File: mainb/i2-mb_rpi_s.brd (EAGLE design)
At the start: 110 x 106.6 mm, 36 parts, among them IC3 DS1307Z, T1 BC337, T2 BC337, X9 eth (mb->rpi)

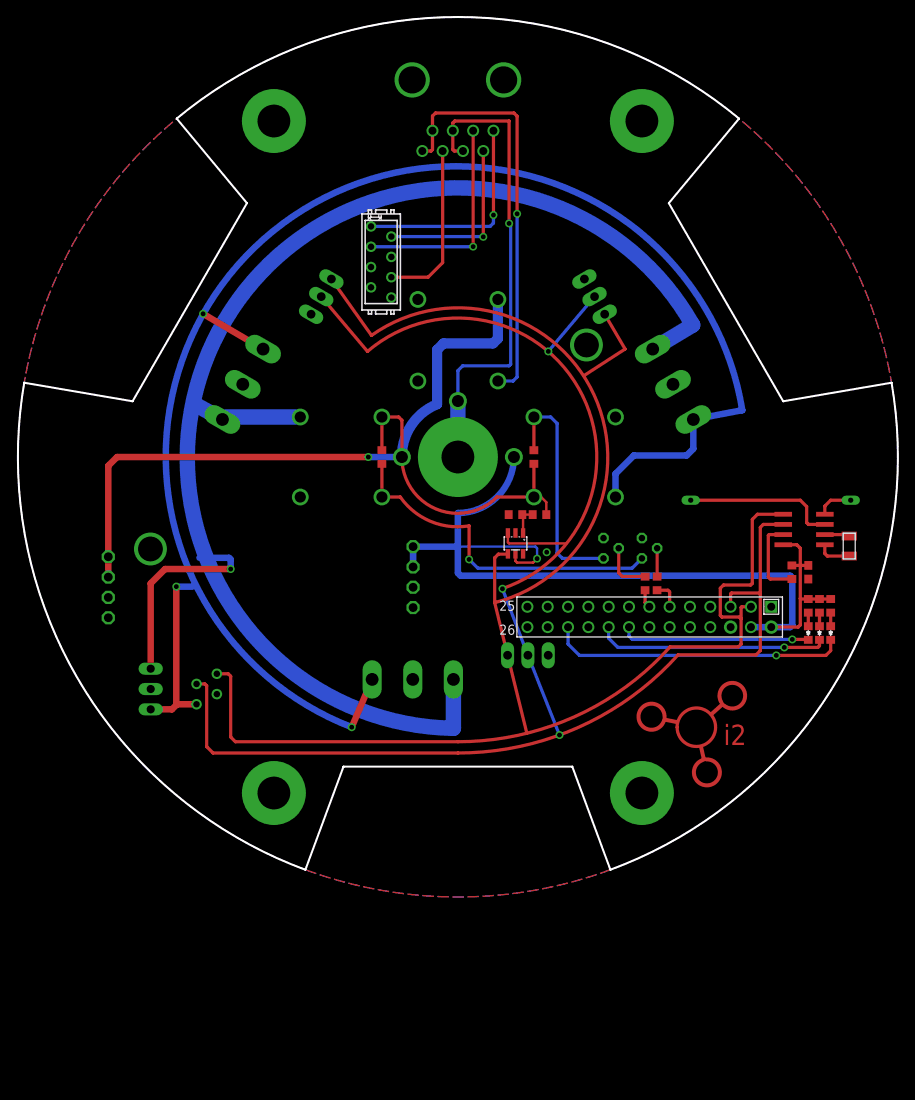
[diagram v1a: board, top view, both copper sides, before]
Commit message: /mainb: 1) pins on relays
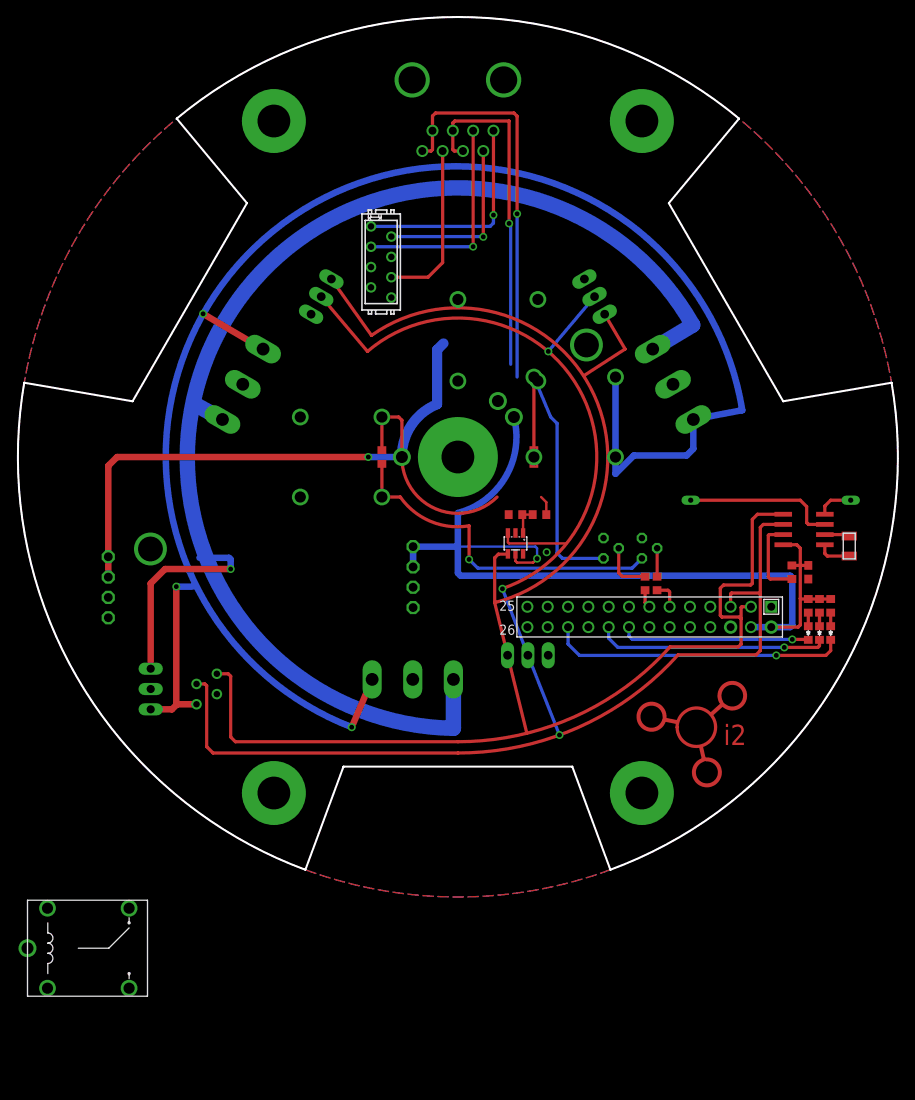
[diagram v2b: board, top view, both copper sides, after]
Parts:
- added U$9: FBR51, wb:PC_RELAY
- moved U$5 5.00 mm to (7.00, 5.00)
- moved U$6 5.00 mm to (5.00, 7.00)
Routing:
- net +12V_IN: track 115.3 -> 94.6 mm
- net AKU+: track 60.0 -> 42.3 mm
- net +12V_OUT: track 110.7 -> 101.3 mm
- net +5V: track 124.7 -> 133.9 mm
- net N$2: track 29.7 -> 38.0 mm
- net +5V_RPI: track 115.6 -> 119.6 mm
- net POE-: track 51.6 -> 49.0 mm
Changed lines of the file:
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@@
 <?xml version="1.0" encoding="utf-8"?>
 <!DOCTYPE eagle SYSTEM "eagle.dtd">
-<eagle version="6.4">
+<eagle version="6.5.0">
 <drawing>
 <settings>
@@
 <element name="R1" library="rcl" package="R0603" value="? 1%" x="10.2" y="-7.2" smashed="yes" rot="R180"/>
 <element name="R2" library="rcl" package="R0603" value="? 1%" x="7.2" y="-7.2" smashed="yes" rot="R180"/>
-<element name="U$6" library="wb" package="PC_RELAY" value="FBR51" x="0" y="7" smashed="yes" rot="MR90"/>
+<element name="U$6" library="wb" package="PC_RELAY" value="FBR51" x="5" y="7" smashed="yes" rot="MR90"/>
 <element name="U$7" library="wb" package="PC_RELAY" value="FBR51" x="-7" y="0" smashed="yes" rot="MR0"/>
 <element name="X_ETH" library="con-maritex" package="8P8C-TOP" value="eth (PC-&gt;mb)" x="0" y="44.6" smashed="yes" rot="R90"/>
 <element name="R3" library="rcl" package="R0603" value="4k7" x="23.4" y="-15.8" smashed="yes" rot="R90"/>
 <element name="U$3" library="wojtkowa" package="D0603" value="1N4148" x="9.5" y="0" smashed="yes" rot="R270"/>
-<element name="U$5" library="wb" package="PC_RELAY" value="FBR51" x="7" y="0" smashed="yes" rot="MR180"/>
+<element name="U$5" library="wb" package="PC_RELAY" value="FBR51" x="7" y="5" smashed="yes" rot="MR180"/>
 <element name="U$8" library="pololu" package="POLOLU-2111" value="POLOLU-2111" x="-25.92" y="-15.01" smashed="yes" rot="MR180"/>
 <element name="IC3" library="ds1307_pcf8583" package="SOIC8" value="DS1307Z" x="43.27" y="-9.06" smashed="yes" rot="R90">
@@
 </element>
 <element name="U$1" library="isfar2-logo" package="I2-LOGO" value="" x="30" y="-33.4"/>
+<element name="U$9" library="wb" package="PC_RELAY" value="FBR51" x="-53.8" y="-61.4"/>
 </elements>
 <signals>
@@
 <contactref element="X_ETH" pad="8"/>
 <contactref element="U$6" pad="C+"/>
-<wire x1="5" y1="9.5" x2="6.9" y2="9.5" width="0.4064" layer="16"/>
-<wire x1="6.9" y1="9.5" x2="7.4" y2="10" width="0.4064" layer="16"/>
+<wire x1="10" y1="9.5" x2="6.9" y2="9.5" width="0" layer="19" extent="1-16"/>
+<wire x1="6.9" y1="9.5" x2="7.4" y2="10" width="0" layer="19" extent="1-16"/>
 <wire x1="7.4" y1="10" x2="7.4" y2="30.4" width="0.4064" layer="16"/>
 <via x="7.4" y="30.4" extent="1-16" drill="0.6"/>
@@
 <wire x1="-2.6" y1="6.6" x2="-2.6" y2="13.4" width="1.27" layer="16"/>
 <wire x1="-2.6" y1="13.4" x2="-1.8" y2="14.2" width="1.27" layer="16"/>
-<wire x1="-1.8" y1="14.2" x2="4.4" y2="14.2" width="1.27" layer="16"/>
-<wire x1="4.4" y1="14.2" x2="5" y2="14.8" width="1.27" layer="16"/>
-<wire x1="5" y1="19.7" x2="5" y2="14.8" width="1.27" layer="16"/>
 <wire x1="-43.7" y1="-15.01" x2="-43.7" y2="-12.47" width="0.8128" layer="1"/>
 <wire x1="-43.7" y1="-12.47" x2="-43.7" y2="-1.1" width="0.8128" layer="1"/>
@@
 <wire x1="-7" y1="0" x2="-2.6" y2="6.6" width="1.27" layer="16" curve="-68.498566"/>
 <wire x1="-9.5" y1="5" x2="-9.5" y2="0.85" width="0.4064" layer="1"/>
-<wire x1="9.5" y1="-0.85" x2="9.5" y2="-5" width="0.4064" layer="1"/>
-<wire x1="9.5" y1="-5" x2="4.9" y2="-5" width="0.4064" layer="1"/>
+<wire x1="9.5" y1="-0.85" x2="9.5" y2="0" width="0.4064" layer="1"/>
+<wire x1="9.5" y1="0" x2="4.9" y2="-5" width="0" layer="19" extent="1-16"/>
 <wire x1="-7" y1="0" x2="4.9" y2="-5" width="0.4064" layer="1" curve="135.578726"/>
 <wire x1="-7" y1="0" x2="-7" y2="4.6" width="0.4064" layer="1"/>
@@
 <wire x1="10.4" y1="-5" x2="11.05" y2="-5.65" width="0.3048" layer="1"/>
 <wire x1="11.05" y1="-7.2" x2="11.05" y2="-5.65" width="0.3048" layer="1"/>
-<wire x1="10.4" y1="-5" x2="9.5" y2="-5" width="0.3048" layer="1"/>
+<wire x1="10.4" y1="-5" x2="9.5" y2="0" width="0" layer="19" extent="1-16"/>
+<wire x1="-1.8" y1="14.2" x2="0" y2="19.7" width="0" layer="19" extent="16-16"/>
 </signal>
 <signal name="+5V" airwireshidden="yes">
@@
 <wire x1="-24.35" y1="13.48940625" x2="-31.85" y2="17.9" width="0.8128" layer="1"/>
 <via x="-31.85" y="17.9" extent="1-16" drill="0.6"/>
-<wire x1="19.7" y1="-5" x2="19.7" y2="-2.1" width="0.8128" layer="16"/>
+<wire x1="19.7" y1="10" x2="19.7" y2="-2.1" width="0.8128" layer="16"/>
 <wire x1="19.7" y1="-2.1" x2="22" y2="0.2" width="0.8128" layer="16"/>
 <wire x1="22" y1="0.2" x2="28.6" y2="0.2" width="0.8128" layer="16"/>
@@
 <contactref element="I2C_3" pad="3"/>
 <contactref element="I2C_1" pad="3"/>
+<wire x1="8.15" y1="-12.1001" x2="7.2" y2="-9.4999" width="0" layer="19" extent="1-1"/>
 </signal>
 <signal name="N$1">
@@
 <contactref element="U$5" pad="C-"/>
 <contactref element="T2" pad="3"/>
-<wire x1="9.5" y1="5" x2="9.5" y2="0.85" width="0.4064" layer="1"/>
+<wire x1="9.5" y1="10" x2="9.5" y2="0.85" width="0.4064" layer="1"/>
 <wire x1="18.2" y1="-12.67" x2="13.07" y2="-12.67" width="0.4064" layer="16"/>
 <wire x1="13.07" y1="-12.67" x2="12.4" y2="-12" width="0.4064" layer="16"/>
 <wire x1="12.4" y1="-12" x2="12.4" y2="4.2" width="0.4064" layer="16"/>
 <wire x1="12.4" y1="4.2" x2="11.6" y2="5" width="0.4064" layer="16"/>
-<wire x1="9.5" y1="5" x2="11.6" y2="5" width="0.4064" layer="16"/>
+<wire x1="9.5" y1="10" x2="11.6" y2="5" width="0.4064" layer="16"/>
 </signal>
 <signal name="REL1">
@@
 <contactref element="X_ETH" pad="5"/>
 <via x="0" y="0" extent="1-16" drill="4.1" diameter="10"/>
-<wire x1="0" y1="0" x2="0" y2="7" width="1.9304" layer="16"/>
-<wire x1="0" y1="7" x2="0" y2="10.8" width="0.4064" layer="16"/>
-<wire x1="0" y1="10.8" x2="0.6" y2="11.4" width="0.4064" layer="16"/>
-<wire x1="0.6" y1="11.4" x2="6.4" y2="11.4" width="0.4064" layer="16"/>
-<wire x1="6.4" y1="11.4" x2="6.6" y2="11.6" width="0.4064" layer="16"/>
+<wire x1="0" y1="0" x2="5" y2="7" width="0" layer="19" extent="1-16"/>
+<wire x1="5" y1="7" x2="0" y2="10.8" width="0" layer="19" extent="1-16"/>
+<wire x1="0" y1="10.8" x2="0.6" y2="11.4" width="0" layer="19" extent="1-16"/>
+<wire x1="0.6" y1="11.4" x2="6.4" y2="11.4" width="0" layer="19" extent="1-16"/>
+<wire x1="6.4" y1="11.4" x2="6.6" y2="11.6" width="0" layer="19" extent="1-16"/>
 <wire x1="6.6" y1="11.6" x2="6.6" y2="29" width="0.4064" layer="16"/>
 <wire x1="6.6" y1="29" x2="6.4" y2="29.2" width="0.4064" layer="16"/>
@@
 <wire x1="-5.6" y1="-13.74" x2="-5.6" y2="-11.2" width="0.8128" layer="16"/>
 <wire x1="-5.6" y1="-11.2" x2="0" y2="-11.2" width="0.8128" layer="16"/>
-<wire x1="7" y1="0" x2="0" y2="-7" width="0.8128" layer="16" curve="-90"/>
+<wire x1="7" y1="5" x2="0" y2="-7" width="0.8128" layer="16" curve="-90"/>
 <wire x1="0" y1="-11.2" x2="0" y2="-7" width="0.8128" layer="16"/>
 <wire x1="41.8" y1="-21" x2="41.8" y2="-15.1" width="0.8128" layer="16"/>
@@
 <wire x1="23.92" y1="-18.72" x2="23.4" y2="-18.2" width="0.4064" layer="1"/>
 </signal>
-<signal name="+12V_OUT" airwireshidden="yes">
+<signal name="+12V_OUT">
 <contactref element="U$7" pad="NO"/>
 <contactref element="PWR4" pad="3"/>
@@
 <wire x1="24.350003125" y1="13.48940625" x2="29.35" y2="16.5" width="1.9304" layer="16"/>
 <wire x1="-0.56" y1="-33.91" x2="29.35" y2="16.5" width="1.9304" layer="16" curve="-239.633819"/>
-<wire x1="-19.7" y1="5" x2="-29.12059375" y2="5" width="1.9304" layer="16"/>
 <wire x1="-29.12059375" y1="5" x2="-29.430003125" y2="4.690590625" width="1.27" layer="16"/>
 <wire x1="-38.4" y1="-26.46" x2="-38.4" y2="-15.8" width="0.8128" layer="1"/>
@@
 <wire x1="-28.4" y1="-12.8" x2="-28.6" y2="-12.6" width="0.8128" layer="16"/>
 <wire x1="-28.6" y1="-12.6" x2="-32.3" y2="-12.6" width="0.8128" layer="16"/>
-<wire x1="-29.430003125" y1="4.690590625" x2="-28.6" y2="-12.6" width="0" layer="19" extent="16-16"/>
-<wire x1="-0.56" y1="-27.8" x2="-28.4" y2="-14" width="0" layer="19" extent="1-1"/>
+<wire x1="-19.7" y1="-5" x2="-28.4" y2="-12.8" width="0" layer="19" extent="16-16"/>
+<wire x1="-29.430003125" y1="4.690590625" x2="-19.7" y2="-5" width="0" layer="19" extent="1-1"/>
+<wire x1="-0.56" y1="-27.8" x2="-19.7" y2="-5" width="0" layer="19" extent="1-1"/>
 </signal>
 <signal name="LED2">

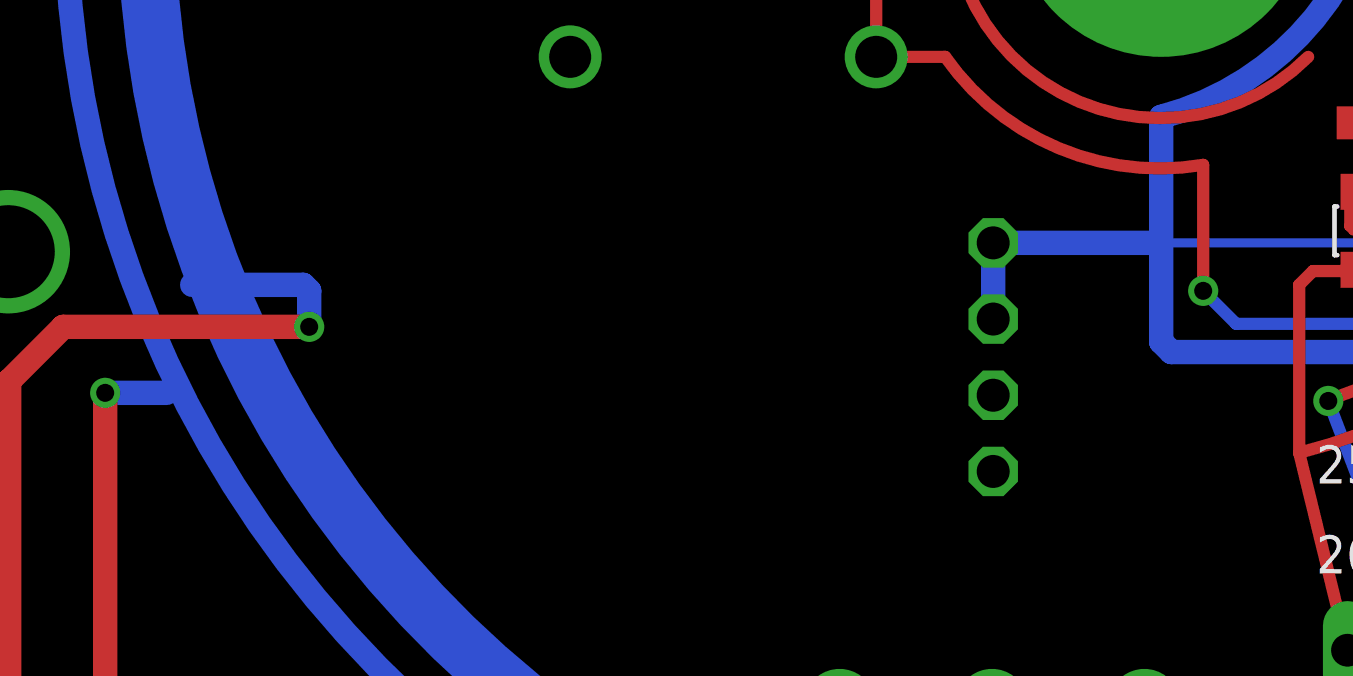
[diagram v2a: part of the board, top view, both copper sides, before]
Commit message: mainb: 3) volt.reg. package dim.
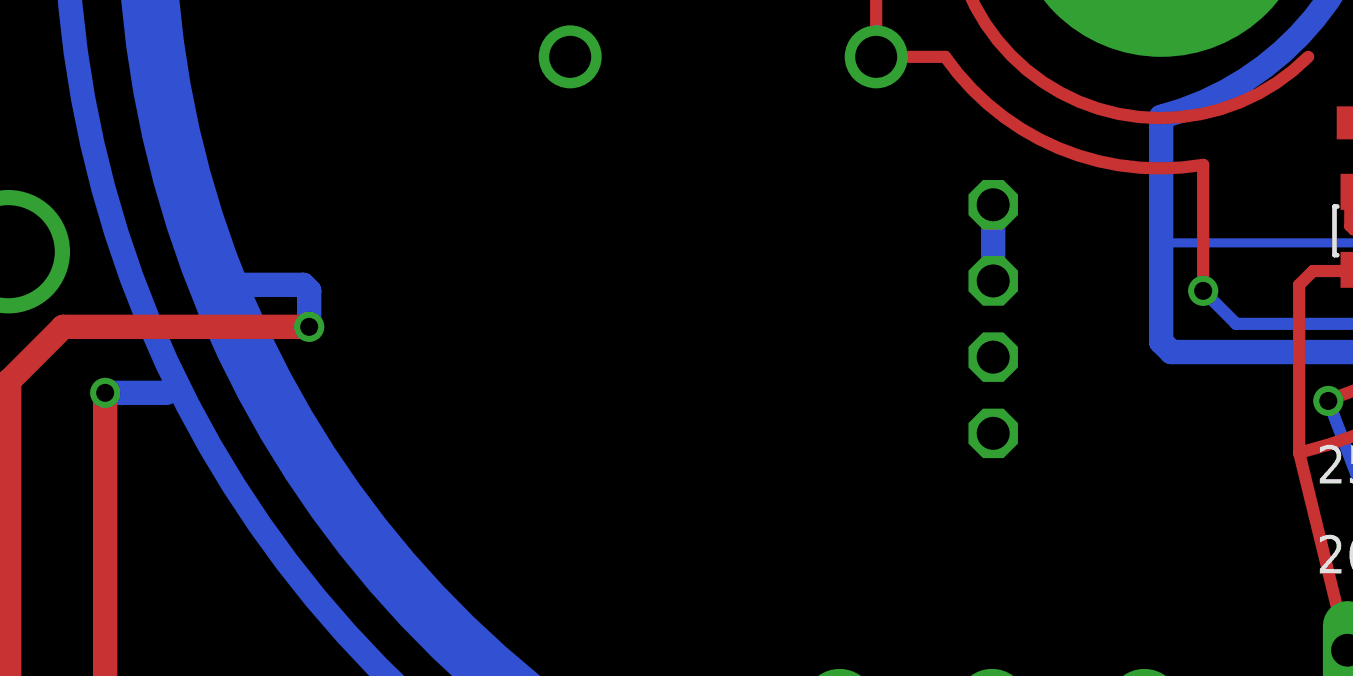
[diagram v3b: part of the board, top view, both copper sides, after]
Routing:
- net +5V_RPI: track 119.6 -> 114.0 mm
- net +12V_OUT: track 101.3 -> 100.7 mm
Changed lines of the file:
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@@
 <contactref element="X_ETH" pad="8"/>
 <contactref element="U$6" pad="C+"/>
-<wire x1="10" y1="9.5" x2="6.9" y2="9.5" width="0" layer="19" extent="1-16"/>
-<wire x1="6.9" y1="9.5" x2="7.4" y2="10" width="0" layer="19" extent="1-16"/>
 <wire x1="7.4" y1="10" x2="7.4" y2="30.4" width="0.4064" layer="16"/>
 <via x="7.4" y="30.4" extent="1-16" drill="0.6"/>
@@
 <wire x1="-3.35" y1="38.25" x2="-3.175" y2="38.425" width="0.4064" layer="1"/>
 <wire x1="-3.175" y1="40.79" x2="-3.175" y2="38.425" width="0.4064" layer="1"/>
+<wire x1="7.4" y1="10" x2="10" y2="9.5" width="0" layer="19" extent="16-16"/>
 </signal>
 <signal name="TX+">
@@
 <wire x1="-9.5" y1="5" x2="-9.5" y2="0.85" width="0.4064" layer="1"/>
 <wire x1="9.5" y1="-0.85" x2="9.5" y2="0" width="0.4064" layer="1"/>
-<wire x1="9.5" y1="0" x2="4.9" y2="-5" width="0" layer="19" extent="1-16"/>
 <wire x1="-7" y1="0" x2="4.9" y2="-5" width="0.4064" layer="1" curve="135.578726"/>
 <wire x1="-7" y1="0" x2="-7" y2="4.6" width="0.4064" layer="1"/>
@@
 <wire x1="10.4" y1="-5" x2="11.05" y2="-5.65" width="0.3048" layer="1"/>
 <wire x1="11.05" y1="-7.2" x2="11.05" y2="-5.65" width="0.3048" layer="1"/>
-<wire x1="10.4" y1="-5" x2="9.5" y2="0" width="0" layer="19" extent="1-16"/>
 <wire x1="-1.8" y1="14.2" x2="0" y2="19.7" width="0" layer="19" extent="16-16"/>
+<wire x1="10.4" y1="-5" x2="4.9" y2="-5" width="0" layer="19" extent="1-1"/>
+<wire x1="9.5" y1="-0.85" x2="10.4" y2="-5" width="0" layer="19" extent="1-1"/>
 </signal>
 <signal name="+5V" airwireshidden="yes">
@@
 <contactref element="I2C_3" pad="3"/>
 <contactref element="I2C_1" pad="3"/>
-<wire x1="8.15" y1="-12.1001" x2="7.2" y2="-9.4999" width="0" layer="19" extent="1-1"/>
 </signal>
 <signal name="N$1">
@@
 <contactref element="X_ETH" pad="5"/>
 <via x="0" y="0" extent="1-16" drill="4.1" diameter="10"/>
-<wire x1="0" y1="0" x2="5" y2="7" width="0" layer="19" extent="1-16"/>
-<wire x1="5" y1="7" x2="0" y2="10.8" width="0" layer="19" extent="1-16"/>
-<wire x1="0" y1="10.8" x2="0.6" y2="11.4" width="0" layer="19" extent="1-16"/>
-<wire x1="0.6" y1="11.4" x2="6.4" y2="11.4" width="0" layer="19" extent="1-16"/>
-<wire x1="6.4" y1="11.4" x2="6.6" y2="11.6" width="0" layer="19" extent="1-16"/>
 <wire x1="6.6" y1="11.6" x2="6.6" y2="29" width="0.4064" layer="16"/>
 <wire x1="6.6" y1="29" x2="6.4" y2="29.2" width="0.4064" layer="16"/>
@@
 <wire x1="-0.45" y1="38.25" x2="-0.635" y2="38.435" width="0.4064" layer="1"/>
 <wire x1="-0.635" y1="40.79" x2="-0.635" y2="38.435" width="0.4064" layer="1"/>
+<wire x1="5" y1="7" x2="6.6" y2="11.6" width="0" layer="19" extent="16-16"/>
+<wire x1="0" y1="0" x2="5" y2="7" width="0" layer="19" extent="1-1"/>
 </signal>
 <signal name="+5V_RPI">
@@
 <contactref element="U$2" pad="2"/>
 <contactref element="IC3" pad="8"/>
-<wire x1="-5.6" y1="-13.74" x2="-5.6" y2="-11.2" width="0.8128" layer="16"/>
-<wire x1="-5.6" y1="-11.2" x2="0" y2="-11.2" width="0.8128" layer="16"/>
+<wire x1="-5.6" y1="-12.47" x2="-5.6" y2="-9.93" width="0.8128" layer="16"/>
 <wire x1="7" y1="5" x2="0" y2="-7" width="0.8128" layer="16" curve="-90"/>
 <wire x1="0" y1="-11.2" x2="0" y2="-7" width="0.8128" layer="16"/>
@@
 <wire x1="43.8" y1="-17.75" x2="42.85" y2="-17.75" width="0.4064" layer="1"/>
 <wire x1="42.85" y1="-17.75" x2="42.8" y2="-17.7" width="0.4064" layer="1"/>
+<wire x1="0" y1="-11.2" x2="-5.6" y2="-12.47" width="0" layer="19" extent="16-16"/>
 </signal>
 <signal name="N$3">
@@
 <wire x1="-28.4" y1="-14" x2="-28.4" y2="-12.8" width="0.8128" layer="16"/>
 <wire x1="-28.4" y1="-12.8" x2="-28.6" y2="-12.6" width="0.8128" layer="16"/>
-<wire x1="-28.6" y1="-12.6" x2="-32.3" y2="-12.6" width="0.8128" layer="16"/>
+<wire x1="-28.6" y1="-12.6" x2="-31.7" y2="-12.6" width="0.8128" layer="16"/>
 <wire x1="-19.7" y1="-5" x2="-28.4" y2="-12.8" width="0" layer="19" extent="16-16"/>
 <wire x1="-29.430003125" y1="4.690590625" x2="-19.7" y2="-5" width="0" layer="19" extent="1-1"/>
